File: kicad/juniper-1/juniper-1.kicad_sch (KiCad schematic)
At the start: 53 parts, among them J1 BOOT_OPTION, J2 UART, J3 ENCODER, J4 BATT_INPUT, J5 1714984, Q1 NTMFS5C645NL, Q2 NTMFS5C645NL, Q3 NTMFS5C645NL, Q4 NTMFS5C645NL, Q5 NTMFS5C645NL, Q6 NTMFS5C645NL, SW1 SW1, U1 TMC6200-TA, U2 ESP32-S2-WROOM, U4 TXB0102, U5 LDL1117S33R

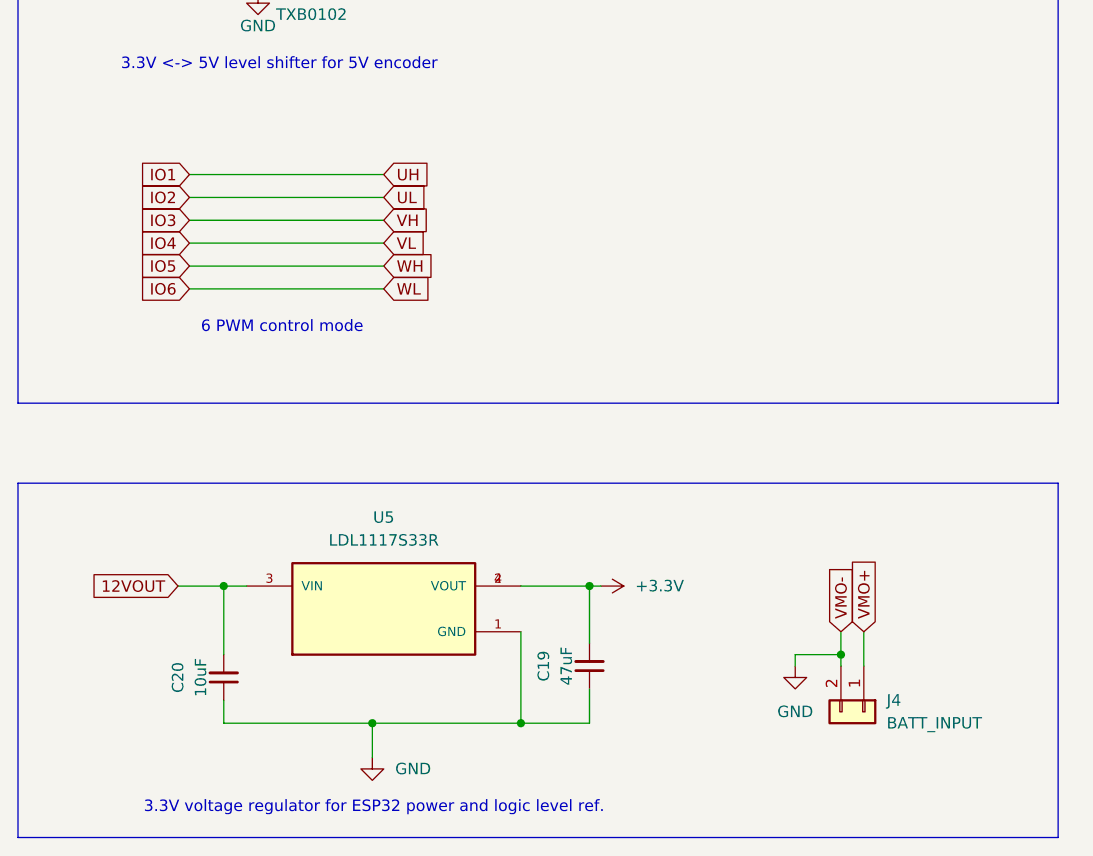
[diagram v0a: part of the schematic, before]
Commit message: added schematic, started routing
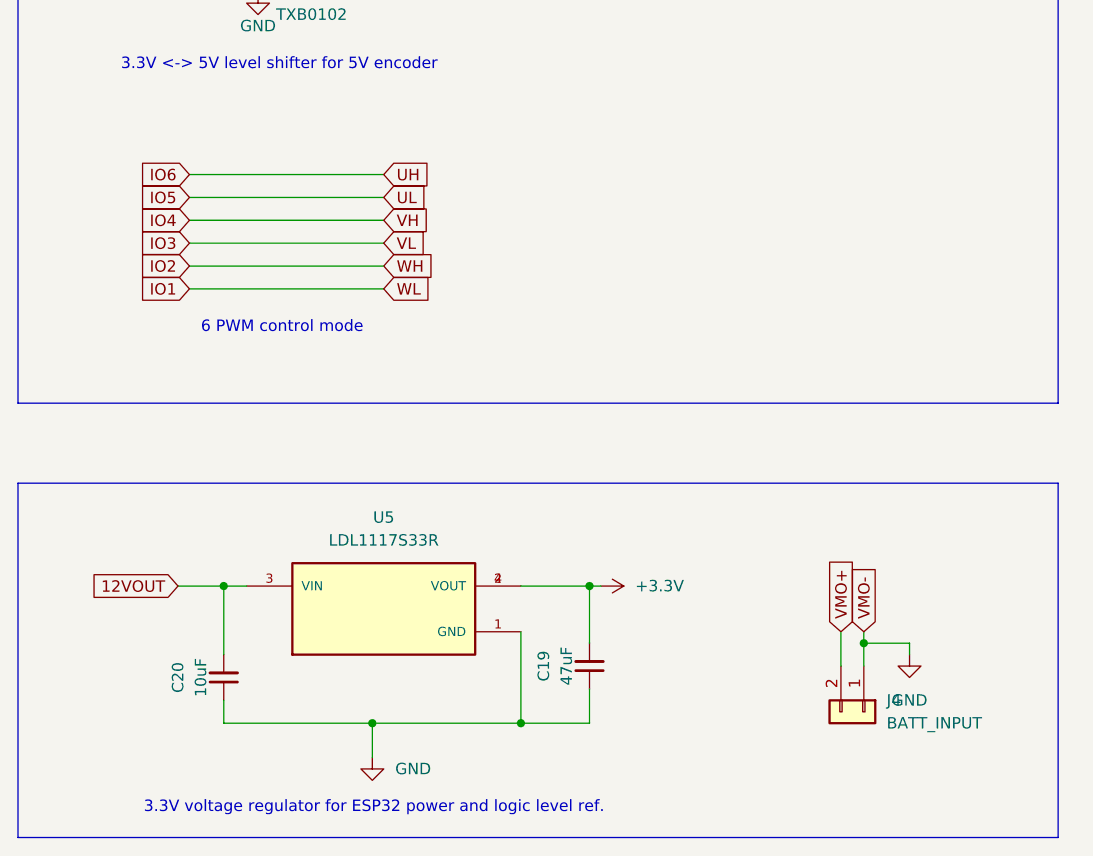
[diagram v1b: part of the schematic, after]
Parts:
- J5: footprint 1714984 -> 1714984:1714984
- Q1, Q2, Q3, Q4, Q5, Q6: footprint TRANS_NTMFS5C628NLT1G -> NTMFS5C628NLT1G:TRANS_NTMFS5C628NLT1G
- U1: footprint eTQFP48_9x9_TRI -> footprints:TMC6200-TA
- U2: footprint XCVR_ESP32-S2-WROOM -> ESP32-S2-WROOM:XCVR_ESP32-S2-WROOM
- U5: footprint SOT230P700X180-4N -> LDL1117S30R:SOT230P700X180-4N
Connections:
- net GND: now also J4.1 (Pin_1); no longer J4.2 (Pin_2)
- net IO1: now also U1.23 (WL); no longer U1.17 (UH)
- net IO2: now also U1.22 (WH); no longer U1.18 (UL)
- net IO3: now also U1.21 (VL); no longer U1.20 (VH)
- net IO4: now also U1.20 (VH); no longer U1.21 (VL)
- net IO5: now also U1.18 (UL); no longer U1.22 (WH)
- net IO6: now also U1.17 (UH); no longer U1.23 (WL)
- net VMO+: now also J4.2 (Pin_2); no longer J4.1 (Pin_1)

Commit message: removed current sense for now...
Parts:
- removed R10, R15, R5: 10, Resistor_SMD:R_0603_1608Metric_Pad0.98x0.95mm_HandSolder, symbol Device:R_Small
- J4: footprint Connector_AMASS:AMASS_XT60-F_1x02_P7.20mm_Vertical -> Connector_AMASS:AMASS_XT60-M_1x02_P7.20mm_Vertical
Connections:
- net USENSE: no longer names the net of U1.46 (USENSE)
- net VSENSE: no longer names the net of U1.41 (VSENSE)
- net WSENSE: no longer names the net of U1.39 (WSENSE)
- no-connect marks 27 -> 30

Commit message: .
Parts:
- removed R1: 10K, Resistor_SMD:R_0603_1608Metric_Pad0.98x0.95mm_HandSolder, symbol Device:R_Small
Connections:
- net VMO+ is gone; now on net GND: C1.1, C10.1, C15.1, C2.1, C3.1, C4.1, C8.2, J4.2 (Pin_2), Q1.5, Q3.5, Q5.5, U1.29 (VSA), U1.33 (VS)
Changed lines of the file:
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@@
     (stroke (width 0) (type default) (color 0 0 0 0))
   )
-  (wire (pts (xy 104.14 83.82) (xy 104.14 85.09))
+  (wire (pts (xy 99.06 82.55) (xy 104.14 82.55))
     (stroke (width 0) (type default) (color 0 0 0 0))
   )
@@
     (stroke (width 0) (type default) (color 0 0 0 0))
   )
-  (wire (pts (xy 375.92 44.45) (xy 375.92 45.72))
-    (stroke (width 0) (type default) (color 0 0 0 0))
-  )
   (wire (pts (xy 170.18 40.64) (xy 179.07 40.64))
     (stroke (width 0) (type default) (color 0 0 0 0))
@@
     (stroke (width 0) (type default) (color 0 0 0 0))
   )
+  (wire (pts (xy 104.14 82.55) (xy 104.14 85.09))
+    (stroke (width 0) (type default) (color 0 0 0 0))
+  )
   (wire (pts (xy 300.99 77.47) (xy 314.96 77.47))
     (stroke (width 0) (type default) (color 0 0 0 0))
@@
     (stroke (width 0) (type default) (color 0 0 0 0))
   )
-  (wire (pts (xy 375.92 38.1) (xy 375.92 39.37))
+  (wire (pts (xy 375.92 38.1) (xy 375.92 45.72))
     (stroke (width 0) (type default) (color 0 0 0 0))
   )
@@
     (pin "1")
   )
-  (symbol (lib_id "Device:R_Small") (at 375.92 41.91 0) (unit 1)
-    (in_bom yes) (on_board yes)
-    (property "Reference" "R1" (id 0) (at 381 41.91 90))
-    (property "Value" "10K" (id 1) (at 378.46 41.91 90))
-    (property "Footprint" "Resistor_SMD:R_0603_1608Metric_Pad0.98x0.95mm_HandSolder" (id 2) (at 375.92 41.91 0)
-      (effects (font (size 1.27 1.27)) hide)
-    )
-    (property "Datasheet" "~" (id 3) (at 375.92 41.91 0)
-      (effects (font (size 1.27 1.27)) hide)
-    )
-    (pin "1")
-    (pin "2")
-  )
   (symbol (lib_id "Device:C_Small") (at 88.9 250.19 180) (unit 1)
     (in_bom yes) (on_board yes)
@@
     (pin "4")
   )
-  (symbol (lib_id "power:GND") (at 104.14 83.82 180) (unit 1)
-    (in_bom yes) (on_board yes)
-    (property "Reference" "#PWR08" (id 0) (at 104.14 77.47 0)
-      (effects (font (size 1.27 1.27)) hide)
-    )
-    (property "Value" "GND" (id 1) (at 104.14 78.74 0))
-    (property "Footprint" "" (id 2) (at 104.14 83.82 0)
-      (effects (font (size 1.27 1.27)) hide)
-    )
-    (property "Datasheet" "" (id 3) (at 104.14 83.82 0)
+  (symbol (lib_id "power:GND") (at 99.06 82.55 0) (unit 1)
+    (in_bom yes) (on_board yes)
+    (property "Reference" "#PWR08" (id 0) (at 99.06 88.9 0)
+      (effects (font (size 1.27 1.27)) hide)
+    )
+    (property "Value" "GND" (id 1) (at 99.06 87.63 0))
+    (property "Footprint" "" (id 2) (at 99.06 82.55 0)
+      (effects (font (size 1.27 1.27)) hide)
+    )
+    (property "Datasheet" "" (id 3) (at 99.06 82.55 0)
       (effects (font (size 1.27 1.27)) hide)
     )
@@
       (reference "Q6") (unit 1) (value "NTMFS5C645NL") (footprint "NTMFS5C628NLT1G:TRANS_NTMFS5C628NLT1G")
     )
-    (path "/8e236c20-075b-42c1-91e3-60b2dfd7bf43"
-      (reference "R1") (unit 1) (value "10K") (footprint "Resistor_SMD:R_0603_1608Metric_Pad0.98x0.95mm_HandSolder")
-    )
     (path "/4ba50183-fcd8-428d-9b57-b33247eb0c4e"
